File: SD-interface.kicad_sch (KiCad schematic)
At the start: 13 parts, among them J7 SD_Card_Receptacle, U15 GL3224-OIY04, Y2 25MHz +-0.03%

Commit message: TPS25762 EEPROM connector added
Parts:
- renumbered J7 to J8
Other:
- title: (none) -> USB Hub
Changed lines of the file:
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@@
 	(generator_version "9.0")
 	(paper "A4")
+	(title_block
+		(title "USB Hub")
+	)
 	(bus_alias "USB3"
 		(members "TX1+" "TX1-" "RX1+" "RX1-" "D+" "D-")
@@
 		(dnp no)
 		(fields_autoplaced yes)
-		(property "Reference" "J7"
+		(property "Reference" "J8"
 			(at 209.1533 30.48 0)
 			(effects
@@
 			(project ""
 				(path "/a2586c28-95f1-49e6-9254-37d7a8473e53/9b23769b-d955-4774-b8ac-278fd96aa141"
-					(reference "J7")
+					(reference "J8")
 					(unit 1)
 				)

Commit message: deleted duplicated capacitor
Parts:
- C69, C70, C71, C72, C73, C74, C75, C76: footprint (none) -> Capacitor_SMD:C_0402_1005Metric
- D1: footprint (none) -> Diode_SMD:D_0603_1608Metric
- J8: footprint (none) -> Connector_Card:SD_Kyocera_145638009511859+
- R44: footprint (none) -> Resistor_SMD:R_0603_1608Metric
- Y2: footprint (none) -> Crystal:Crystal_SMD_0603-4Pin_6.0x3.5mm
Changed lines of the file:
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@@
 			)
 		)
-		(property "Footprint" ""
+		(property "Footprint" "Capacitor_SMD:C_0402_1005Metric"
 			(at 18.7452 63.5 0)
 			(effects
@@
 			)
 		)
-		(property "Footprint" ""
+		(property "Footprint" "Capacitor_SMD:C_0402_1005Metric"
 			(at 46.0248 107.95 0)
 			(effects
@@
 			)
 		)
-		(property "Footprint" ""
+		(property "Footprint" "Connector_Card:SD_Kyocera_145638009511859+"
 			(at 215.9 56.642 0)
 			(effects
@@
 			)
 		)
-		(property "Footprint" ""
+		(property "Footprint" "Capacitor_SMD:C_0402_1005Metric"
 			(at 42.8752 41.91 0)
 			(effects
@@
 			)
 		)
-		(property "Footprint" ""
+		(property "Footprint" "Capacitor_SMD:C_0402_1005Metric"
 			(at 25.0952 41.91 0)
 			(effects
@@
 			)
 		)
-		(property "Footprint" ""
+		(property "Footprint" "Capacitor_SMD:C_0402_1005Metric"
 			(at 33.9852 41.91 0)
 			(effects
@@
 			)
 		)
-		(property "Footprint" ""
+		(property "Footprint" "Capacitor_SMD:C_0402_1005Metric"
 			(at 21.8948 107.95 0)
 			(effects
@@
 			)
 		)
-		(property "Footprint" ""
+		(property "Footprint" "Resistor_SMD:R_0603_1608Metric"
 			(at 36.83 80.518 90)
 			(effects
@@
 			)
 		)
-		(property "Footprint" ""
+		(property "Footprint" "Crystal:Crystal_SMD_0603-4Pin_6.0x3.5mm"
 			(at 35.56 106.68 0)
 			(effects
@@
 			)
 		)
-		(property "Footprint" ""
+		(property "Footprint" "Capacitor_SMD:C_0402_1005Metric"
 			(at 27.6352 63.5 0)
 			(effects
@@
 			)
 		)
-		(property "Footprint" ""
+		(property "Footprint" "Diode_SMD:D_0603_1608Metric"
 			(at 80.01 102.87 0)
 			(effects
@@
 			)
 		)
-		(property "Footprint" ""
+		(property "Footprint" "Capacitor_SMD:C_0402_1005Metric"
 			(at 16.2052 41.91 0)
 			(effects

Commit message: Minor fixes
Fixed unclear labelling of buses
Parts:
- R44: footprint Resistor_SMD:R_0603_1608Metric -> Resistor_SMD:R_0402_1005Metric
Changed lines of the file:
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@@
 			)
 		)
-		(property "Footprint" "Resistor_SMD:R_0603_1608Metric"
+		(property "Footprint" "Resistor_SMD:R_0402_1005Metric"
 			(at 36.83 80.518 90)
 			(effects

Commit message: MCP19035 changed to MP8795
TPS7A4701xRGW to AP7361C-33E
Led Indicator added
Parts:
- added C118, C119: 330nF, Capacitor_SMD:C_0402_1005Metric, symbol Device:C_Small
- added R84: R, symbol Device:R
- added U31, U32: TPD4E02B04DQA, Package_SON:USON-10_2.5x1.0mm_P0.5mm, symbol Snapeda:TPD4E02B04DQA
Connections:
- net GND: now also U31.3 (G), U31.8 (G), U32.3 (G), U32.8 (G)
- net LED: now also R84.1; no longer D1.2 (A)
- net SD_CD: now also U32.4 (IO3), U32.7 (NC)
- net SD_CK: now also U32.1 (IO1), U32.10 (NC)
- net SD_CM: now also U32.2 (IO2), U32.9 (NC)
- net SD_D0: now also U31.1 (IO1), U31.10 (NC)
- net SD_D1: now also U31.2 (IO2), U31.9 (NC)
- net SD_D2: now also U31.4 (IO3), U31.7 (NC)
- net SD_D3: now also U31.5 (IO4), U31.6 (NC)
- net SD_WP: now also U32.5 (IO4), U32.6 (NC)
- net USB-SD.TX1+: now also C119.1; no longer U15.2 (TXP)
- net USB-SD.TX1-: now also C118.1; no longer U15.1 (TXN)
- new net: C119.2, U15.2 (TXP)
- new net: C118.2, U15.1 (TXN)
- new net: D1.2 (A), R84.2
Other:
- moved on the sheet: C69, C70, C71, C72

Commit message: Ferrite bread filter for LDO and MIC23201, labelling improved
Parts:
- D1: value LED -> GREEN
- R84: value R -> 520
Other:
- note added: "ESD Protection"
- note added: "Memory card access LED"
- note added: "SD Port"
- moved on the sheet: D1, J8, R84

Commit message: Schematic reannotated
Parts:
- renumbered C69 to C70, C70 to C71, C71 to C72, C72 to C73, C118 to C74, C119 to C75, C73 to C76, C74 to C77, C75 to C78, C76 to C79, D1 to D5, R44 to R58, R84 to R59, U31 to U16, U32 to U17

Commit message: J11 changed to 8-pin PCIe connector, footprint assigned
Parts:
- R59: footprint (none) -> Resistor_SMD:R_0402_1005Metric
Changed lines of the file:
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@@
 			)
 		)
-		(property "Footprint" ""
+		(property "Footprint" "Resistor_SMD:R_0402_1005Metric"
 			(at 74.93 113.538 90)
 			(effects

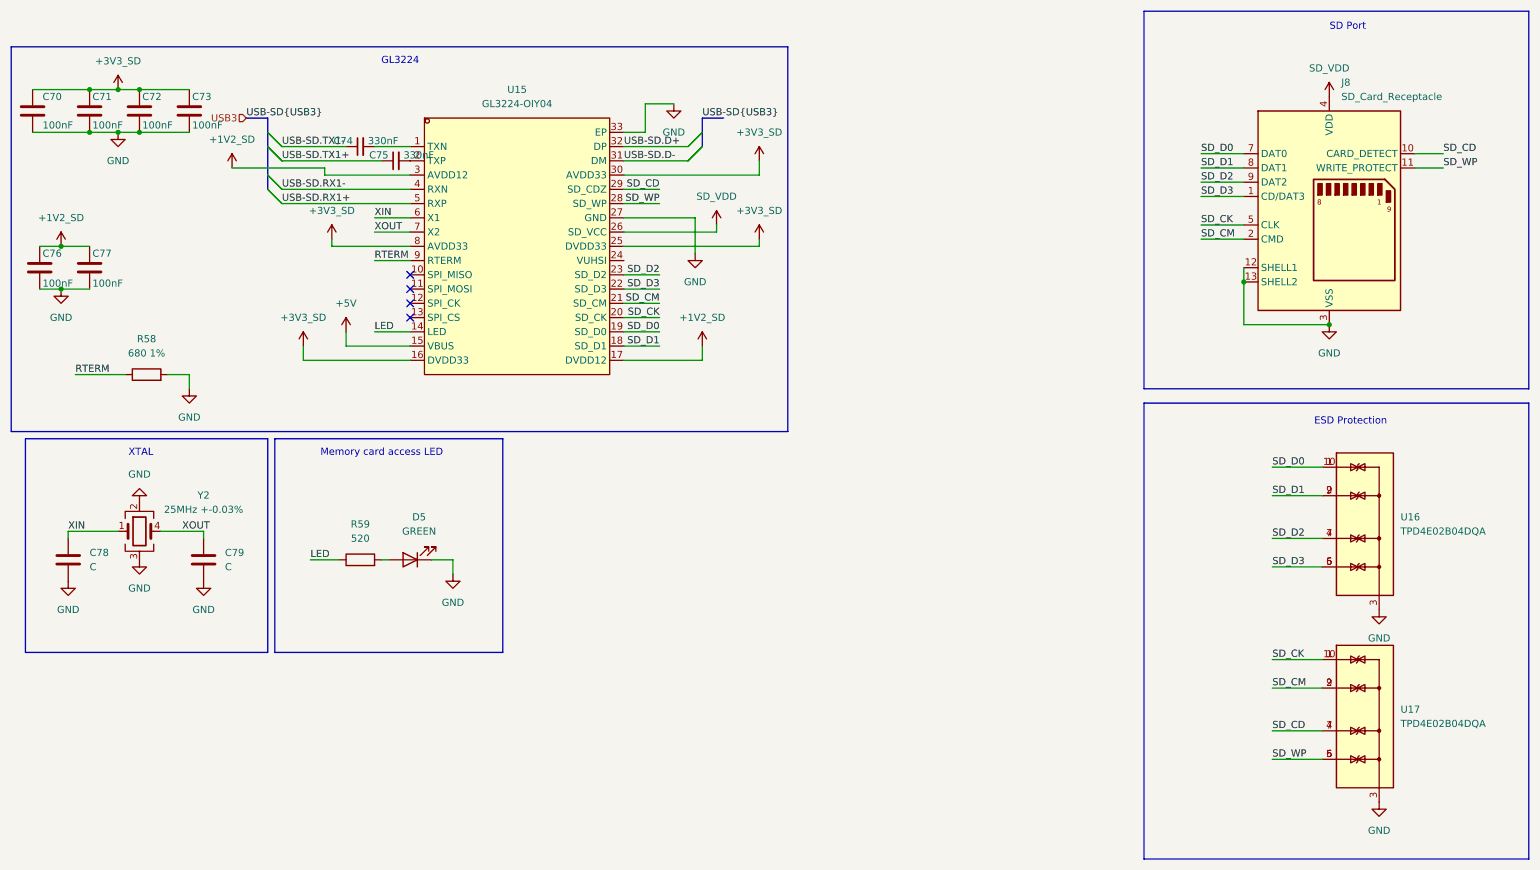
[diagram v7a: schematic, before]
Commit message: Net class for USB SS signals created and applied on schematic
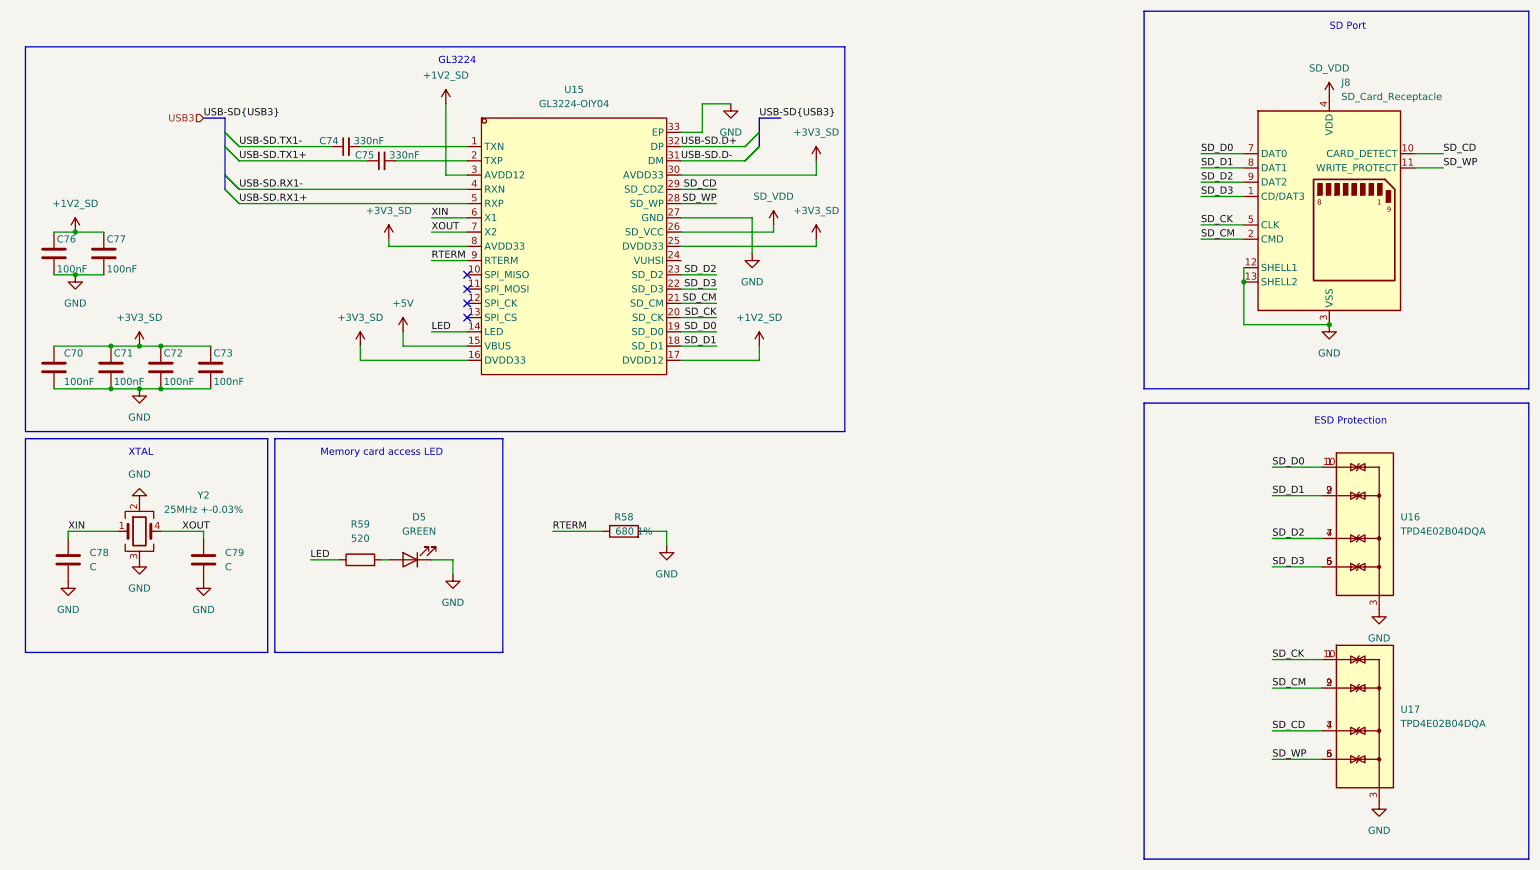
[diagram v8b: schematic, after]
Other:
- moved on the sheet: C70, C71, C72, C73, C74, C75, C76, C77, R58, U15
